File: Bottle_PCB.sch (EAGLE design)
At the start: 105 parts, among them Q1 8.000 MHz, Q2 ZVN 3306 F, Q3 ZVN 3306 F, Q4 ZVN 3306 F, Q5 ZVN 3306 F, Q6 ZVN 3306 F, Q7 ZVN 3306 F, U1 USD-SOCKETNEW

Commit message: - Added Arduino Shield headers - cleaned up the schmeatic and grouped modules on sheets by function - inserted and de-crossed bus systems - started to unify font sizes and pin / netwrok naming
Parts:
- removed SJ5, SJ6, SJ7, SJ8: (no value), jumper:SJ2W
- added AD: (no value), con-lsta:FE06-1
- added IOH: (no value), con-lsta:FE10-1
- added IOL, POWER: (no value), con-lsta:FE08-1
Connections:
- net VBATT_AIN0 renamed PB2_VBATT_AIN0
- net VBATT_AIN1 renamed PB3_VBATT_AIN1
- removed net INT_BUTTON: ATMEGA1284.(PCINT9/CLKO/T1)PB1, C12.2, SW_WAKEUP.P, SW_WAKEUP.P1
- removed net N$20: ATMEGA1284.(PCINT6/ADC6)PA6, SJ4.1
- removed net N$24: SJ5.2, U1.DO
- removed net N$25: ATMEGA1284.(PCINT7/ADC7)PA7, SJ3.1
- removed net N$26: Q2.S, SJ6.2
- removed net N$27: Q3.S, SJ7.2
- removed net N$5: C_U12V.+, LM2594_3.3.IN, R10.1, SV2.9, SV3.9, T_U12V.S
- removed net PB4/SS: ATMEGA1284.(PCINT12/OC0B/!SS!)PB4, SJ8.1
- removed net PB5/MOSI: ATMEGA1284.(PCINT13/MOSI)PB5, ISP1.MOSI, SJ7.1
- removed net PB6/MISO: ATMEGA1284.(PCINT14/MISO)PB6, ISP1.MISO, SJ5.1
- removed net PB7/SCK: ATMEGA1284.(PCINT15/SCK)PB7, ISP1.SCK, SJ6.1
- removed net PC0/I2C_SDL: ATMEGA1284.(PCINT16/SCL)PC0, I2C.3, R4.1
- removed net PC1/I2C_SDA: ATMEGA1284.(PCINT17/SDA)PC1, I2C.2, R3.1
- removed net PD5/CS: ATMEGA1284.(PCINT29/OC1A)PD5, SJ8.3
- removed net RXD1/MISO: ATMEGA1284.(PCINT26/INT0)PD2, SJ5.3
- removed net SD_CS: Q4.S, SJ8.2
- removed net TXD1/MOSI: ATMEGA1284.(PCINT27/INT1)PD3, SJ7.3
- removed net USB_BT_RXD0: ATMEGA1284.(PCINT24/RXD0)PD0, TP1.TP, UART1_IC2.RXD, XB1.DOUT
- removed net USB_BT_TXD0: ATMEGA1284.(PCINT25/TXD0)PD1, R9.2, UART1_IC2.TXD
- removed net XCK1/SCK: ATMEGA1284.(PCINT28/OC1B)PD4, SJ6.3
- new net +5V: POWER.2, POWER.5
- new net N$7: SJ3.1
- new net PA0: AD.1, ATMEGA1284.(PCINT0/ADC0)PA0
- new net PA1: AD.2, ATMEGA1284.(PCINT1/ADC1)PA1
- new net PA2: AD.3, ATMEGA1284.(PCINT2/ADC2)PA2
- new net PA3: AD.4, ATMEGA1284.(PCINT3/ADC3)PA3
- new net PA4: AD.5, ATMEGA1284.(PCINT4/ADC4)PA4
- new net PA5: AD.6, ATMEGA1284.(PCINT5/ADC5)PA5
- new net PA6: SJ4.1
- new net PB0: ATMEGA1284.(PCINT8/XCK0/T0)PB0, IOH.1
- new net PB1_INT_BUTTON: ATMEGA1284.(PCINT9/CLKO/T1)PB1, C12.2, IOH.2, SW_WAKEUP.P, SW_WAKEUP.P1
- new net PB4_SS: ATMEGA1284.(PCINT12/OC0B/!SS!)PB4, IOH.3
- new net PB5_MOSI: ATMEGA1284.(PCINT13/MOSI)PB5, IOH.4, ISP1.MOSI
- new net PB6_MISO: ATMEGA1284.(PCINT14/MISO)PB6, IOH.5, ISP1.MISO
- new net PB7_SCK: ATMEGA1284.(PCINT15/SCK)PB7, IOH.6, ISP1.SCK
- new net PC0_I2C_SDL: ATMEGA1284.(PCINT16/SCL)PC0, I2C.3, IOH.10, R4.1
- new net PC1_I2C_SDA: ATMEGA1284.(PCINT17/SDA)PC1, I2C.2, IOH.9, R3.1
- new net PD0_RXD0_USB: ATMEGA1284.(PCINT24/RXD0)PD0, UART1_IC2.RXD
- new net PD0_RXD0_USB_BT: IOL.1, TP1.TP, XB1.DOUT
- new net PD1_TXD0_USB: ATMEGA1284.(PCINT25/TXD0)PD1, IOL.2, R9.2, UART1_IC2.TXD
- new net PD2_RXD1/MISO: ATMEGA1284.(PCINT26/INT0)PD2, IOL.3, U1.DO
- new net PD3_TXD1/MOSI: ATMEGA1284.(PCINT27/INT1)PD3, IOL.4, Q3.S
- new net PD4_XCK1/SCK: ATMEGA1284.(PCINT28/OC1B)PD4, IOL.5, Q2.S
- new net PD5_CS: ATMEGA1284.(PCINT29/OC1A)PD5, IOL.6, Q4.S
- new net PD6: ATMEGA1284.(PCINT30/OC2B/ICP)PD6, IOL.7
- new net PD7: ATMEGA1284.(PCINT31/OC2A)PD7, IOL.8
- new net VIN: C_U12V.+, LM2594_3.3.IN, POWER.8, R10.1, SV2.9, SV3.9, T_U12V.S
- net +3V3: now also POWER.4
- net AREF: now also IOH.8
- net BT_MODE: no longer ATMEGA1284.(PCINT0/ADC0)PA0
- net BT_PAIR: no longer ATMEGA1284.(PCINT2/ADC2)PA2
- net BT_RESET: no longer ATMEGA1284.(PCINT3/ADC3)PA3
- net BT_STATUS: no longer ATMEGA1284.(PCINT1/ADC1)PA1
- net BT_VCC_SIGNAL: no longer ATMEGA1284.(PCINT4/ADC4)PA4
- net GND: now also IOH.7, POWER.6, POWER.7
- net RESET: now also POWER.3
- net VBATT: no longer ATMEGA1284.(PCINT5/ADC5)PA5
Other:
- note added: "Arduino Headers"
- note added: "FTDI USB interface"
- note added: "Headers"
- note added: "Main MCU"
- note added: "NC"
- note added: "USB Communication"
- note added: "XBEE Communication"
- moved on the sheet: ATMEGA1284, C1, C10, C11, C12, C16, C2, C3, C4, C5, C6, C7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

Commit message: - employes Seeduino Open Parts Library for groove connectors and possibly more in the future - added groove connectors
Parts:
- removed SJ3, SJ4: (no value), jumper:SJ
- added GROOVE_D7_D8, GROOVE_I2C, J1: GROVE-4P-2.0-SMD, OPL:GROVE-4P-2.0-SMD-FEMALE-REINFORCE-3470090P1
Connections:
- removed net N$7: SJ3.1
- new net PA7: ATMEGA1284.(PCINT7/ADC7)PA7, J1.3
- net +3V3: now also GROOVE_D7_D8.2, GROOVE_I2C.2, J1.2
- net GND: now also GROOVE_D7_D8.1, GROOVE_I2C.1, J1.1
- net N$16: no longer SJ3.2
- net N$17: no longer SJ4.2
- net PA6: now also ATMEGA1284.(PCINT6/ADC6)PA6, J1.4; no longer SJ4.1
- net PB0: now also GROOVE_D7_D8.3
- net PC0_I2C_SDL: now also GROOVE_I2C.3
- net PC1_I2C_SDA: now also GROOVE_I2C.4
- net PD7: now also GROOVE_D7_D8.4
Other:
- note added: "Groove Headers"
- note added: "Power Supply"
- moved on the sheet: C12, C4, C5, C_U12V, C_U5V, D_U5V, LM2594_3.3, L_U5V, Q2, Q3, Q4, Q5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

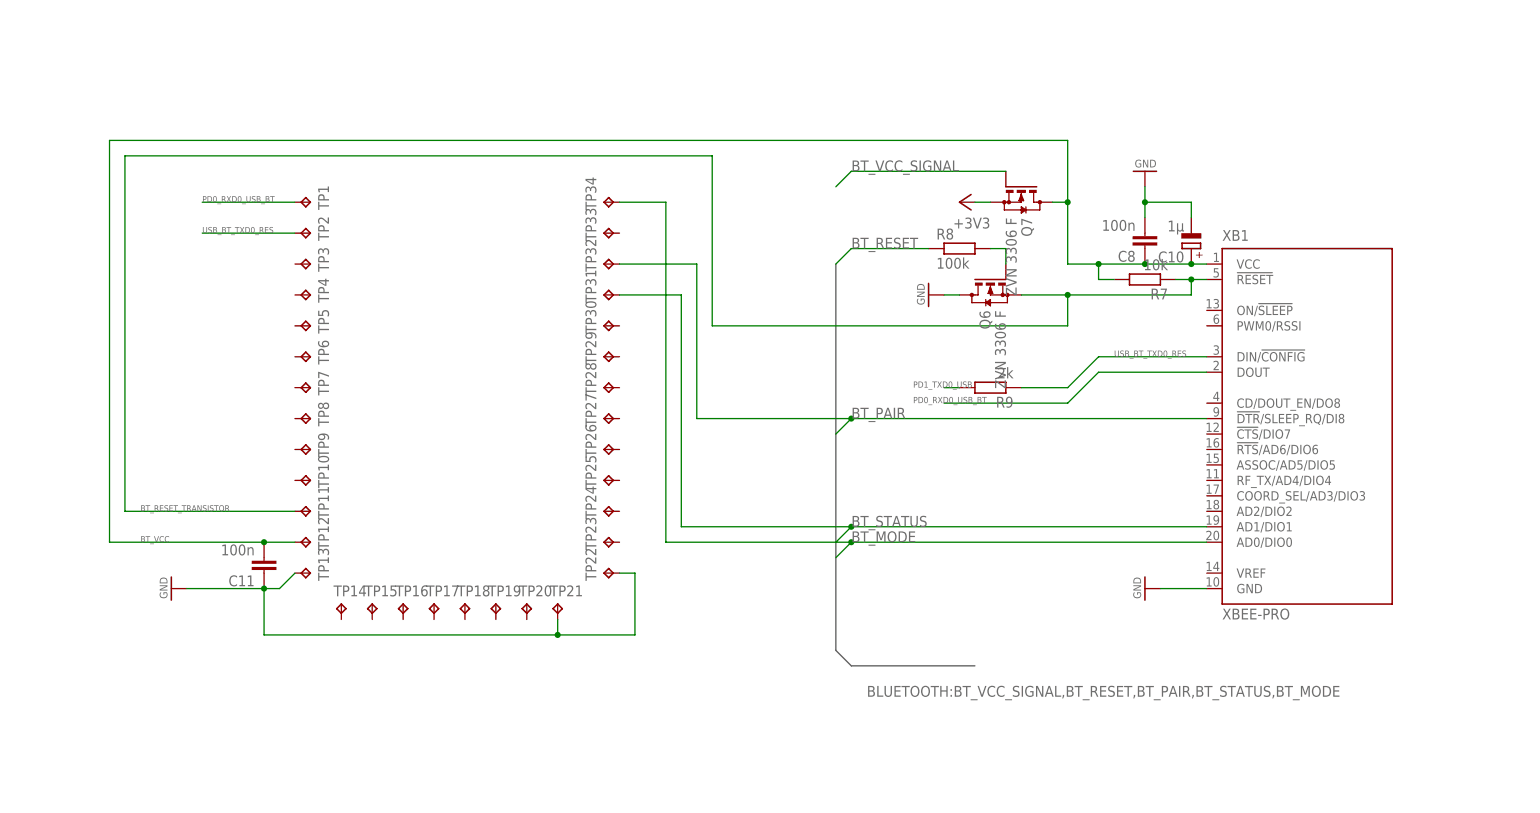
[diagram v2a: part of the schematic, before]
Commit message: - changed old BTBee Pro specific socketing into more generic XBEE socket
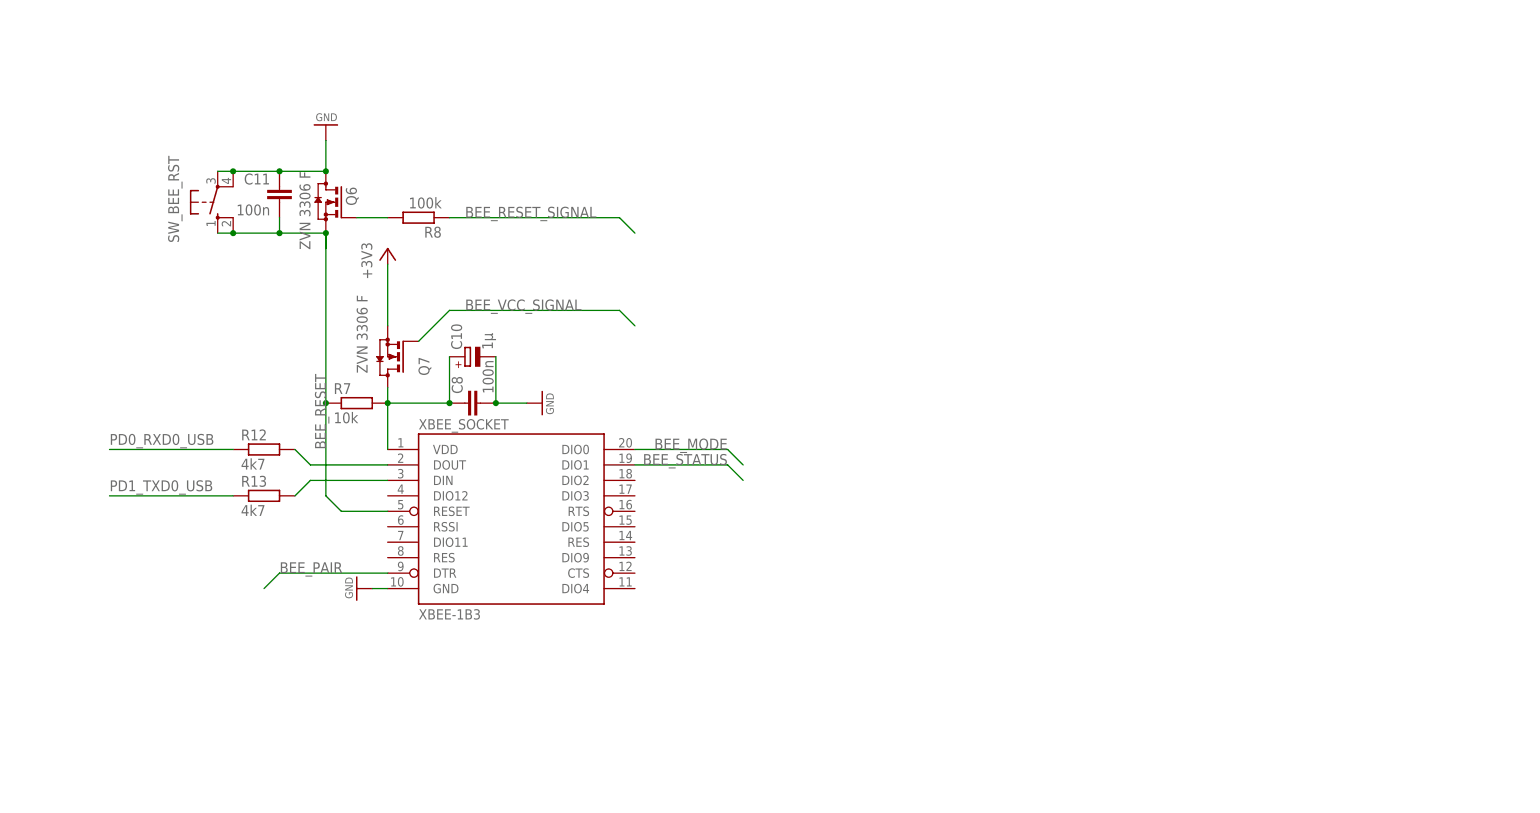
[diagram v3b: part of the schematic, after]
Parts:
- removed R9: 2k, rcl:R-EU_M1206
- removed TP1, TP10, TP11, TP12, TP13, TP14, TP15, TP16, TP17, TP18, TP19, TP2, TP20, TP21, TP22, TP23, TP24, TP25, TP26, TP27, TP28, TP29, TP3, TP30, TP31, TP32, TP33, TP34, TP4, TP5, TP6, TP7, TP8, TP9: TPTP06SQ, testpad:TPTP06SQ
- removed XB1: XBEE-PRO, maxstream:XBEE-PRO
- added R12, R13: 4k7, resistor:R-EU_R0603
- added SW_BEE_RST: (no value), switch-omron:10-XX
- added XBEE_SOCKET: XBEE-1B3, SparkFun-RF:XBEE-1B3
- R8: device rcl:R-EU_M1206 -> resistor:R-EU_R0603
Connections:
- net BT_RESET renamed BEE_RESET_SIGNAL
- net BT_VCC_SIGNAL renamed BEE_VCC_SIGNAL
- removed net BT_MODE: TP34.TP, XB1.AD0/DIO0
- removed net BT_PAIR: TP32.TP, XB1.!DTR!/SLEEP_RQ/DI8
- removed net BT_RESET_TRANSISTOR: Q6.S, R7.1, TP11.TP, XB1.!RESET
- removed net BT_STATUS: TP31.TP, XB1.AD1/DIO1
- removed net BT_VCC: C10.+, C11.2, C8.1, Q7.D, R7.2, TP12.TP, XB1.VCC
- removed net USB_BT_TXD0_RES: R9.1, TP2.TP, XB1.DIN/!CONFIG
- new net BEE_MODE: XBEE_SOCKET.DIO0
- new net BEE_PAIR: XBEE_SOCKET.DTR
- new net BEE_RESET: C11.2, Q6.S, R7.1, SW_BEE_RST.S, SW_BEE_RST.S1, XBEE_SOCKET.RESET
- new net BEE_STATUS: XBEE_SOCKET.DIO1
- new net BEE_VCC: C10.+, C8.1, Q7.D, R7.2, XBEE_SOCKET.VDD
- new net N$15: R13.2, XBEE_SOCKET.DIN
- new net N$8: R12.2, XBEE_SOCKET.DOUT
- net GND: now also SW_BEE_RST.P, SW_BEE_RST.P1, XBEE_SOCKET.GND; no longer TP13.TP, TP21.TP, TP22.TP, XB1.GND
- net PD0_RXD0_USB: now also R12.1
- net PD0_RXD0_USB_BT: no longer TP1.TP, XB1.DOUT
- net PD1_TXD0_USB: now also R13.1; no longer R9.2
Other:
- note added: "XBEE Socket"
- note removed: "HC-05"
- moved on the sheet: C10, C11, C8, Q6, Q7, R7, R8

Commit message: - added FTDI serial connector - employed sparkfun lib for connectors
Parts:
- added JP1: (no value), SparkFun-Connectors:ARDUINO_SERIAL_PROGRAMPTH
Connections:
- net RESET renamed MCU_RST
- removed net DTR#: UART1_D_RESET.C, UART1_IC2.DTR#
- new net FTDI_CTS: JP1.CTS, UART1_IC2.CTS#
- new net FTDI_DTR: JP1.DTR, UART1_D_RESET.C, UART1_IC2.DTR#
- net +3V3: now also JP1.VCC; no longer UART1_C11.1, UART1_C12.+, UART1_IC2.VCC, UART1_L2.2
- net +5V: now also UART1_C11.1, UART1_C12.+, UART1_IC2.VCC, UART1_L2.2
- net GND: now also JP1.GND
- net PD0_RXD0_USB: now also JP1.TXO
- net PD1_TXD0_USB: now also JP1.RXI
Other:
- note added: "FTDI Serial"
- moved on the sheet: I2C, R3, R4, UART1_D_RESET

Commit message: - connected FTDI and XBEE Socket
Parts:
- added R14, R15, R9: 1k, resistor:R-EU_R0603
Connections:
- removed net BEE_PAIR: XBEE_SOCKET.DTR
- new net BEE_DTR: R9.2, XBEE_SOCKET.DTR
- new net FTDI_RTS: R15.2, UART1_IC2.RTS#
- new net N$5: R14.1, XBEE_SOCKET.CTS
- new net N$7: R15.1, XBEE_SOCKET.RTS
- net FTDI_CTS: now also R14.2
- net FTDI_DTR: now also R9.1
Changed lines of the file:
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@@
 <part name="+3V5" library="supply1" deviceset="+3V3" device=""/>
 <part name="+3V17" library="supply1" deviceset="+3V3" device=""/>
+<part name="R9" library="resistor" deviceset="R-EU_" device="R0603" value="1k"/>
+<part name="R14" library="resistor" deviceset="R-EU_" device="R0603" value="1k"/>
+<part name="R15" library="resistor" deviceset="R-EU_" device="R0603" value="1k"/>
 </parts>
 <sheets>
@@
 <text x="151.765" y="286.385" size="0.8128" layer="250" rot="R90">(PDO/MISO)</text>
 <wire x1="368.3" y1="345.44" x2="411.48" y2="345.44" width="0.3048" layer="104" style="shortdash"/>
-<wire x1="287.02" y1="154.94" x2="398.78" y2="154.94" width="0.3048" layer="104" style="shortdash"/>
-<wire x1="398.78" y1="154.94" x2="508" y2="154.94" width="0.3048" layer="104" style="shortdash"/>
+<wire x1="287.02" y1="154.94" x2="419.1" y2="154.94" width="0.3048" layer="104" style="shortdash"/>
+<wire x1="419.1" y1="154.94" x2="508" y2="154.94" width="0.3048" layer="104" style="shortdash"/>
 <wire x1="281.94" y1="149.86" x2="287.02" y2="154.94" width="0.3048" layer="104" style="shortdash" curve="-90"/>
 <wire x1="281.94" y1="48.26" x2="281.94" y2="149.86" width="0.3048" layer="104" style="shortdash"/>
-<wire x1="287.02" y1="43.18" x2="398.78" y2="43.18" width="0.3048" layer="104" style="shortdash"/>
-<wire x1="398.78" y1="43.18" x2="508" y2="43.18" width="0.3048" layer="104" style="shortdash"/>
+<wire x1="287.02" y1="43.18" x2="419.1" y2="43.18" width="0.3048" layer="104" style="shortdash"/>
+<wire x1="419.1" y1="43.18" x2="508" y2="43.18" width="0.3048" layer="104" style="shortdash"/>
 <wire x1="281.94" y1="47.625" x2="286.385" y2="43.18" width="0.3048" layer="104" style="shortdash" curve="90"/>
 <wire x1="288.29" y1="146.05" x2="326.39" y2="146.05" width="0.3048" layer="104"/>
 <text x="289.56" y="147.32" size="3.81" layer="104" font="vector" ratio="12">XBEE Socket</text>
 <wire x1="508" y1="154.94" x2="513.08" y2="149.86" width="0.3048" layer="104" style="shortdash" curve="-90"/>
-<wire x1="398.78" y1="43.18" x2="398.78" y2="154.94" width="0.3048" layer="104" style="shortdash"/>
+<wire x1="419.1" y1="43.18" x2="419.1" y2="154.94" width="0.3048" layer="104" style="shortdash"/>
 <wire x1="513.08" y1="48.26" x2="513.08" y2="149.86" width="0.3048" layer="104" style="shortdash"/>
-<wire x1="407.67" y1="146.05" x2="440.69" y2="146.05" width="0.3048" layer="104"/>
-<text x="408.94" y="147.32" size="3.81" layer="104" font="vector" ratio="12">BTBee Pro</text>
+<wire x1="427.99" y1="146.05" x2="461.01" y2="146.05" width="0.3048" layer="104"/>
+<text x="429.26" y="147.32" size="3.81" layer="104" font="vector" ratio="12">BTBee Pro</text>
 <wire x1="508" y1="43.18" x2="513.08" y2="48.26" width="0.3048" layer="104" style="shortdash" curve="90"/>
 <wire x1="556.26" y1="350.52" x2="678.18" y2="350.52" width="0.3048" layer="104" style="shortdash"/>
@@
 <instance part="+3V5" gate="G$1" x="93.98" y="127" rot="MR90"/>
 <instance part="+3V17" gate="G$1" x="370.84" y="223.52" rot="MR270"/>
+<instance part="R9" gate="G$1" x="312.42" y="68.58"/>
+<instance part="R14" gate="G$1" x="381" y="68.58"/>
+<instance part="R15" gate="G$1" x="381" y="78.74"/>
 </instances>
 <busses>
@@
 <wire x1="393.7" y1="231.14" x2="378.46" y2="231.14" width="0.1524" layer="91"/>
 <label x="378.46" y="231.14" size="1.016" layer="95"/>
+</segment>
+<segment>
+<pinref part="R9" gate="G$1" pin="1"/>
+<wire x1="307.34" y1="68.58" x2="287.02" y2="68.58" width="0.1524" layer="91"/>
+<label x="287.02" y="68.58" size="1.778" layer="95"/>
 </segment>
 </net>
@@
 <pinref part="R13" gate="G$1" pin="1"/>
 <wire x1="307.34" y1="81.28" x2="287.02" y2="81.28" width="0.1524" layer="91"/>
-<label x="287.02" y="83.82" size="1.778" layer="95" rot="MR180"/>
+<label x="287.02" y="81.28" size="1.778" layer="95"/>
 </segment>
 <segment>
@@
 <pinref part="R12" gate="G$1" pin="1"/>
 <wire x1="307.34" y1="88.9" x2="287.02" y2="88.9" width="0.1524" layer="91"/>
-<label x="287.02" y="91.44" size="1.778" layer="95" rot="MR180"/>
+<label x="287.02" y="88.9" size="1.778" layer="95"/>
 </segment>
 <segment>
@@
 <segment>
 <pinref part="XBEE_SOCKET" gate="G$1" pin="DIO1"/>
-<wire x1="388.62" y1="86.36" x2="373.38" y2="86.36" width="0.1524" layer="91"/>
-<label x="388.62" y="86.36" size="1.778" layer="95" rot="MR0"/>
-<wire x1="388.62" y1="86.36" x2="391.16" y2="83.82" width="0.1524" layer="91"/>
+<wire x1="398.78" y1="86.36" x2="373.38" y2="86.36" width="0.1524" layer="91"/>
+<label x="398.78" y="86.36" size="1.778" layer="95" rot="MR0"/>
 </segment>
 </net>
@@
 <segment>
 <pinref part="XBEE_SOCKET" gate="G$1" pin="DIO0"/>
-<wire x1="373.38" y1="88.9" x2="388.62" y2="88.9" width="0.1524" layer="91"/>
-<label x="388.62" y="88.9" size="1.778" layer="95" rot="MR0"/>
-<wire x1="388.62" y1="88.9" x2="391.16" y2="86.36" width="0.1524" layer="91"/>
-</segment>
-</net>
-<net name="BEE_PAIR" class="0">
+<wire x1="373.38" y1="88.9" x2="398.78" y2="88.9" width="0.1524" layer="91"/>
+<label x="398.78" y="88.9" size="1.778" layer="95" rot="MR0"/>
+</segment>
+</net>
+<net name="BEE_DTR" class="0">
 <segment>
 <pinref part="XBEE_SOCKET" gate="G$1" pin="DTR"/>
-<wire x1="332.74" y1="68.58" x2="314.96" y2="68.58" width="0.1524" layer="91"/>
-<wire x1="314.96" y1="68.58" x2="312.42" y2="66.04" width="0.1524" layer="91"/>
-<label x="314.96" y="68.58" size="1.778" layer="95"/>
+<wire x1="332.74" y1="68.58" x2="317.5" y2="68.58" width="0.1524" layer="91"/>
+<label x="317.5" y="68.58" size="1.778" layer="95"/>
+<pinref part="R9" gate="G$1" pin="2"/>
 </segment>
 </net>
@@
 <label x="378.46" y="220.98" size="1.016" layer="95"/>
 </segment>
-</net>
+<segment>
+<pinref part="R14" gate="G$1" pin="2"/>
+<wire x1="386.08" y1="68.58" x2="398.78" y2="68.58" width="0.1524" layer="91"/>
+<label x="398.78" y="68.58" size="1.778" layer="95" rot="MR0"/>
+</segment>
+</net>
+<net name="N$5" class="0">
+<segment>
+<pinref part="XBEE_SOCKET" gate="G$1" pin="CTS"/>
+<wire x1="373.38" y1="68.58" x2="375.92" y2="68.58" width="0.1524" layer="91"/>
+<pinref part="R14" gate="G$1" pin="1"/>
+</segment>
+</net>
+<net name="FTDI_RTS" class="0">
+<segment>
+<pinref part="UART1_IC2" gate="1" pin="RTS#"/>
+<wire x1="58.42" y1="124.46" x2="45.72" y2="124.46" width="0.1524" layer="91"/>
+<label x="45.72" y="124.46" size="1.016" layer="95"/>
+</segment>
+<segment>
+<pinref part="R15" gate="G$1" pin="2"/>
+<wire x1="386.08" y1="78.74" x2="398.78" y2="78.74" width="0.1524" layer="91"/>
+<label x="398.78" y="78.74" size="1.778" layer="95" rot="MR0"/>
+</segment>
+</net>
+<net name="N$7" class="0">
+<segment>
+<pinref part="XBEE_SOCKET" gate="G$1" pin="RTS"/>
+<pinref part="R15" gate="G$1" pin="1"/>
+<wire x1="373.38" y1="78.74" x2="375.92" y2="78.74" width="0.1524" layer="91"/>
+</segment>
+</net>
